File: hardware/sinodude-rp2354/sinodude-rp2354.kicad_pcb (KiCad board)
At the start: 2 copper layers, 75 x 40 mm, 93 parts, among them J1 USB-C, J2 SWD TC2030-IDC latching, J4 DUT, Q1 2N7002, SW1 BOOTSEL, SW2 RESET, U1 RP2354A, U2 AMS1117-3.3, U3 TPS2114APW, U4 SN74LVC8T245PW, U5 SN74LVC1T45DBV, U6 SN74LVC1T45DBV, Y1 12MHz/CL10pF/ESR50R/ABM8-272-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

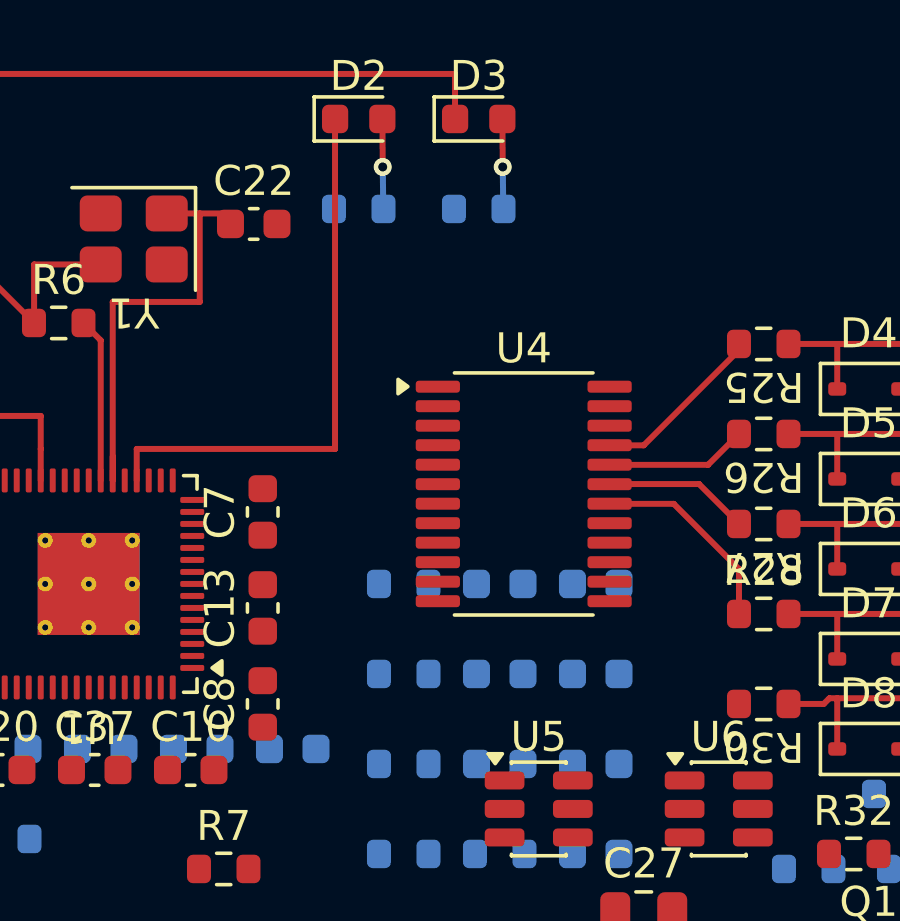
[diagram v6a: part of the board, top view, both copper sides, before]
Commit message: hardware: clear the U1-U4 corridor, route NRST_3V3 and TCK_3V3
Moved C7/C8/C13 out of x=134..140 so the corridor between U1's right pin row
and U4 is clear. Routed NRST_3V3 on top and TCK_3V3 on the bottom through it.

NRST's diagonal originally clipped U4's GND pad 7; it now approaches pin 6
horizontally.

Recorded finding: U1's A-side pin order is the exact reverse of U4's, so the
four-signal bundle has to cross. This is inherent, not a placement mistake -
U1 pin 4 is TCK and pin 8 is NRST, and after the 180 degree rotation that puts
TCK at the bottom of the column while U4 wants it at the top. J4's pin order
matches U4, so the reversal cannot be moved further down the chain either. It
costs roughly 8 vias to resolve in the corridor.

DRC: no shorts, no crossings, no clearance or courtyard violations.
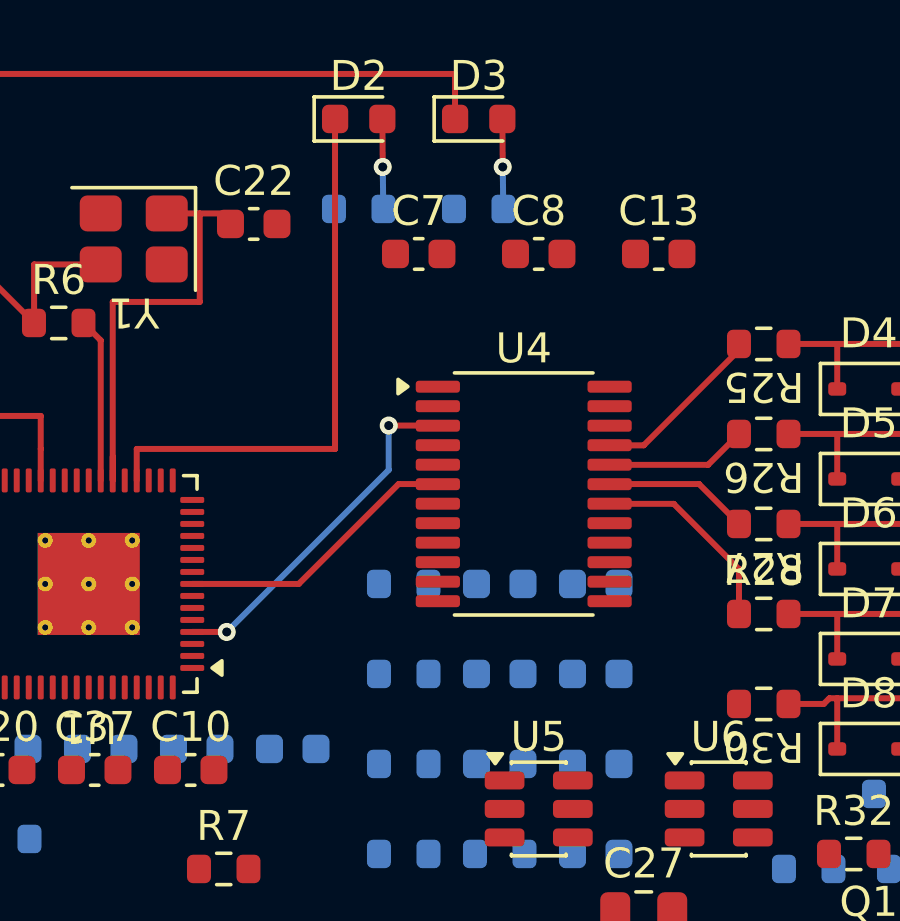
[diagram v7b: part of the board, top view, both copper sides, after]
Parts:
- moved C13 17.7 mm to (149.0, 109.0), turned to 0 degrees
- moved C8 17.6 mm to (145.0, 109.0), turned to 0 degrees
- moved C7 10.0 mm to (141.0, 109.0), turned to 0 degrees
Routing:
- net TCK_3V3: track 0.00 -> 11.9 mm, vias 0 -> 2
- net NRST_3V3: track 0.00 -> 9.57 mm
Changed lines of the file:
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@@
 	(footprint "Capacitor_SMD:C_0603_1608Metric"
 		(layer "F.Cu")
-		(at 135.8 124 90)
+		(at 145 109)
 		(property "Reference" "C8"
-			(at 0 -1.43 90)
+			(at 0 -1.43 0)
 			(unlocked yes)
 			(layer "F.SilkS")
@@
 		)
 		(property "Value" "100nF"
-			(at 0 1.43 90)
+			(at 0 1.43 0)
 			(unlocked yes)
 			(layer "F.SilkS")
@@
 		)
 		(property "Datasheet" ""
-			(at 0 0 90)
+			(at 0 0 0)
 			(layer "F.Fab")
 			(hide yes)
@@
 		)
 		(property "Description" ""
-			(at 0 0 90)
+			(at 0 0 0)
 			(layer "F.Fab")
 			(hide yes)
@@
 		)
 		(fp_text user "${REFERENCE}"
-			(at 0 0 90)
+			(at 0 0 0)
 			(unlocked yes)
 			(layer "F.Fab")
@@
 		)
 		(pad "1" smd roundrect
-			(at -0.775 0 90)
+			(at -0.775 0)
 			(size 0.9 0.95)
 			(layers "F.Cu" "F.Mask" "F.Paste")
@@
 		)
 		(pad "2" smd roundrect
-			(at 0.775 0 90)
+			(at 0.775 0)
 			(size 0.9 0.95)
 			(layers "F.Cu" "F.Mask" "F.Paste")
@@
 	(footprint "Capacitor_SMD:C_0603_1608Metric"
 		(layer "F.Cu")
-		(at 135.8 117.6 90)
+		(at 141 109)
 		(property "Reference" "C7"
-			(at 0 -1.43 90)
+			(at 0 -1.43 0)
 			(unlocked yes)
 			(layer "F.SilkS")
@@
 		)
 		(property "Value" "100nF"
-			(at 0 1.43 90)
+			(at 0 1.43 0)
 			(unlocked yes)
 			(layer "F.SilkS")
@@
 		)
 		(property "Datasheet" ""
-			(at 0 0 90)
+			(at 0 0 0)
 			(layer "F.Fab")
 			(hide yes)
@@
 		)
 		(property "Description" ""
-			(at 0 0 90)
+			(at 0 0 0)
 			(layer "F.Fab")
 			(hide yes)
@@
 		)
 		(fp_text user "${REFERENCE}"
-			(at 0 0 90)
+			(at 0 0 0)
 			(unlocked yes)
 			(layer "F.Fab")
@@
 		)
 		(pad "1" smd roundrect
-			(at -0.775 0 90)
+			(at -0.775 0)
 			(size 0.9 0.95)
 			(layers "F.Cu" "F.Mask" "F.Paste")
@@
 		)
 		(pad "2" smd roundrect
-			(at 0.775 0 90)
+			(at 0.775 0)
 			(size 0.9 0.95)
 			(layers "F.Cu" "F.Mask" "F.Paste")
@@
 	(footprint "Capacitor_SMD:C_0603_1608Metric"
 		(layer "F.Cu")
-		(at 135.8 120.8 90)
+		(at 149 109)
 		(property "Reference" "C13"
-			(at 0 -1.43 90)
+			(at 0 -1.43 0)
 			(unlocked yes)
 			(layer "F.SilkS")
@@
 		)
 		(property "Value" "100nF"
-			(at 0 1.43 90)
+			(at 0 1.43 0)
 			(unlocked yes)
 			(layer "F.SilkS")
@@
 		)
 		(property "Datasheet" ""
-			(at 0 0 90)
+			(at 0 0 0)
 			(layer "F.Fab")
 			(hide yes)
@@
 		)
 		(property "Description" ""
-			(at 0 0 90)
+			(at 0 0 0)
 			(layer "F.Fab")
 			(hide yes)
@@
 		)
 		(fp_text user "${REFERENCE}"
-			(at 0 0 90)
+			(at 0 0 0)
 			(unlocked yes)
 			(layer "F.Fab")
@@
 		)
 		(pad "1" smd roundrect
-			(at -0.775 0 90)
+			(at -0.775 0)
 			(size 0.9 0.95)
 			(layers "F.Cu" "F.Mask" "F.Paste")
@@
 		)
 		(pad "2" smd roundrect
-			(at 0.775 0 90)
+			(at 0.775 0)
 			(size 0.9 0.95)
 			(layers "F.Cu" "F.Mask" "F.Paste")
@@
 	)
 	(segment
+		(start 133.449999 121.6)
+		(end 134.6 121.6)
+		(width 0.2)
+		(layer "F.Cu")
+		(net "TCK_3V3")
+	)
+	(segment
+		(start 140 114.72)
+		(end 141.64 114.72)
+		(width 0.2)
+		(layer "F.Cu")
+		(net "TCK_3V3")
+	)
+	(via
+		(at 134.6 121.6)
+		(size 0.6)
+		(drill 0.3)
+		(layers "F.Cu" "B.Cu")
+		(net "TCK_3V3")
+	)
+	(via
+		(at 140 114.72)
+		(size 0.6)
+		(drill 0.3)
+		(layers "F.Cu" "B.Cu")
+		(net "TCK_3V3")
+	)
+	(segment
+		(start 134.6 121.6)
+		(end 140 116.2)
+		(width 0.2)
+		(layer "B.Cu")
+		(net "TCK_3V3")
+	)
+	(segment
+		(start 140 116.2)
+		(end 140 114.72)
+		(width 0.2)
+		(layer "B.Cu")
+		(net "TCK_3V3")
+	)
+	(segment
+		(start 137 120)
+		(end 140.33 116.67)
+		(width 0.2)
+		(layer "F.Cu")
+		(net "NRST_3V3")
+	)
+	(segment
+		(start 140.33 116.67)
+		(end 141.64 116.67)
+		(width 0.2)
+		(layer "F.Cu")
+		(net "NRST_3V3")
+	)
+	(segment
+		(start 133.449999 120)
+		(end 137 120)
+		(width 0.2)
+		(layer "F.Cu")
+		(net "NRST_3V3")
+	)
+	(segment

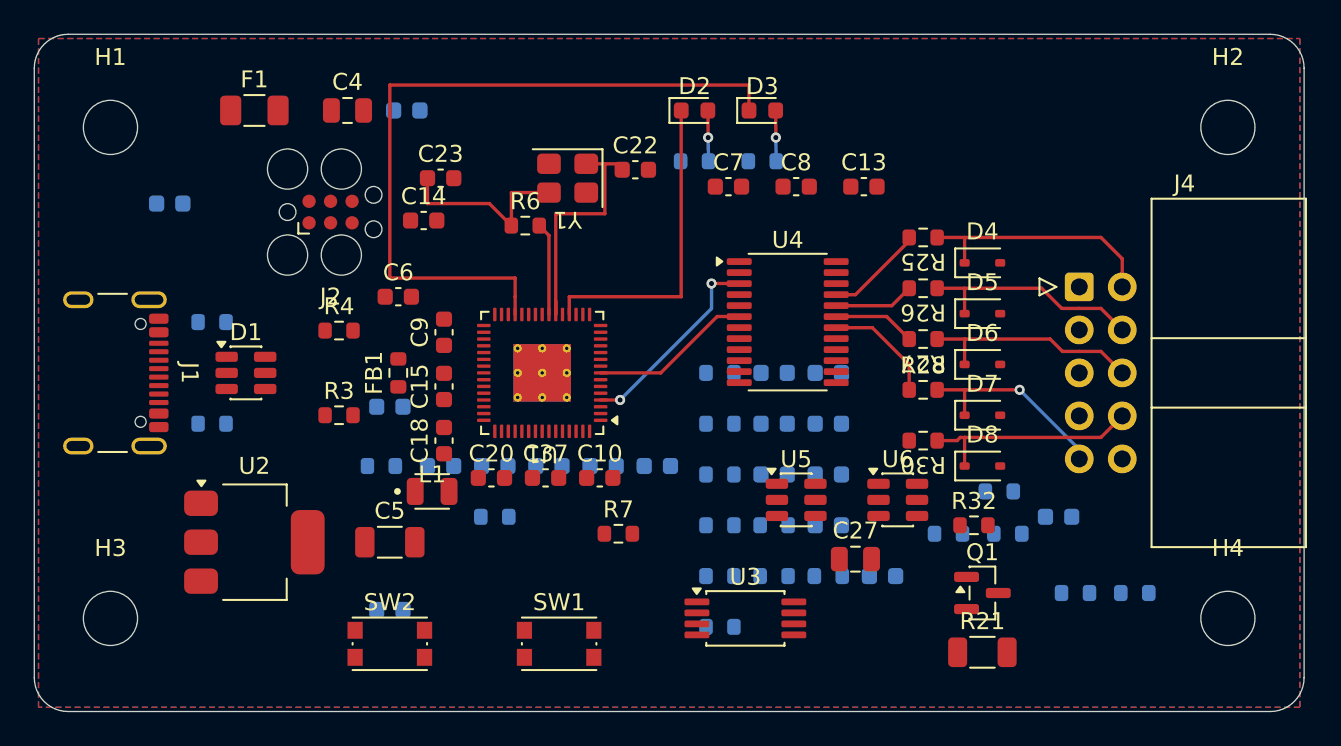
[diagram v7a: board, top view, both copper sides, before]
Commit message: hardware: route 48 links with a scripted geometry router
Built a local router: s-expression parser, pad-position model, spatial
clearance checker, and a 45-degree path search. It computes 128 links needed,
independently matching DRC's 130 unconnected items, and reproduces every pad
position against values previously confirmed over KiCad's live IPC.

Appended 170 segments and 25 vias directly to the board file. Unconnected
drops 130 -> 83.

Three bugs the model-vs-DRC cross-check caught, each validated on a copy
before touching the real board:
- Clearance formula was short by exactly 0.1 mm: trace obstacles were stored
  with w/2 - TW/2, making the requirement CLR + w1/2 + w2/2 - 0.1.
- A 0.15 mm fine-trace fallback undercut the board minimum (37 violations).
- 0.4 mm power traces cannot leave U1's 0.4 mm-pitch pads: centred on a pad,
  a 0.4 mm trace leaves 0.1 mm to its neighbour. Power is now 0.2 mm, which
  still carries the 500 mA the input fuse allows.

Also found: J1's VBUS pins A4/B4 are physically coincident in the USB-C
footprint, so that link needed no trace at all.

DRC: no shorts, no crossings, no clearance and no track-width violations.
Remaining 24 are all pre-existing: U1 thermal via drill, J1 footprint-internal
hole clearance, and thermal-relief spoke counts.
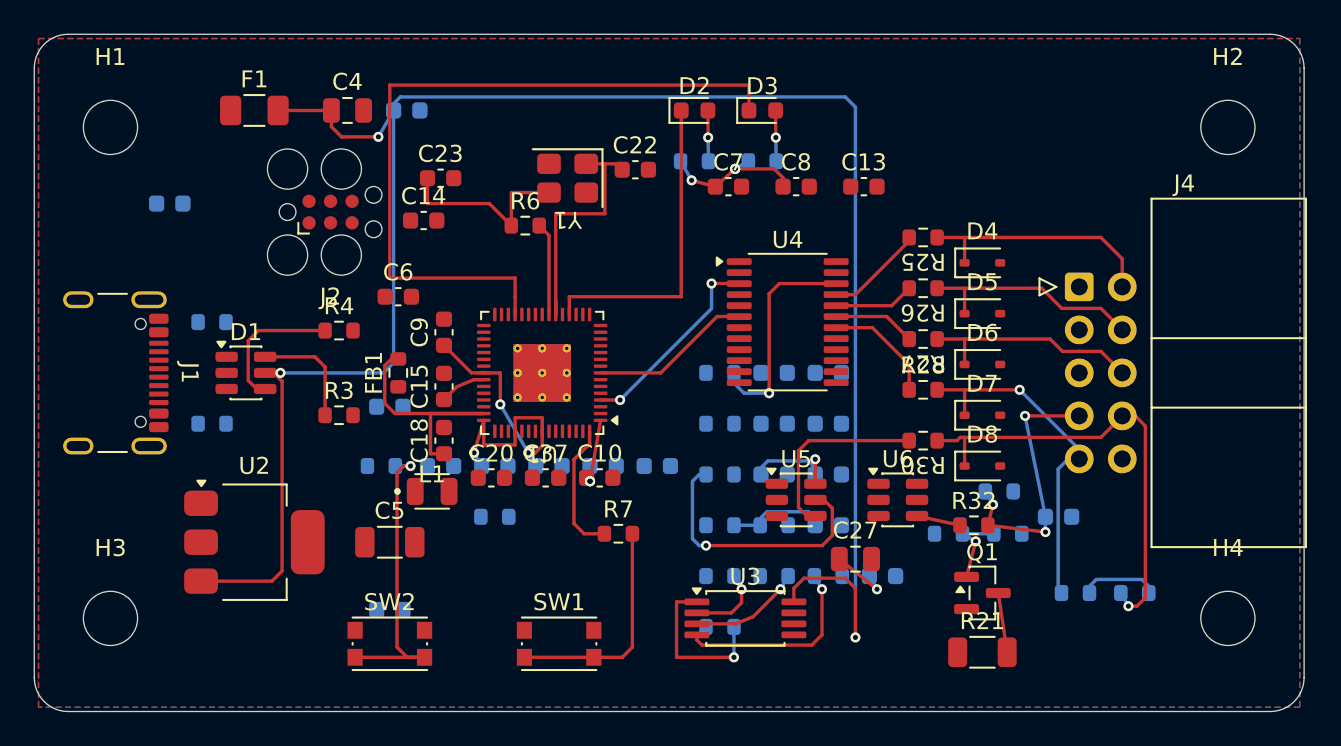
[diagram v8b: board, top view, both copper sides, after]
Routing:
- net +5V: track 0.00 -> 116.4 mm, vias 0 -> 3
- net +3V3: track 0.00 -> 38.4 mm, vias 0 -> 8
- net RUN: track 0.00 -> 18.1 mm, vias 0 -> 1
- net DATA_DIR: track 0.00 -> 15.8 mm, vias 0 -> 1
- net Net-(J4-Pin_7): track 0.00 -> 15.8 mm, vias 0 -> 3
- net ADC_AVDD: track 0.00 -> 15.6 mm
- net VTGT: track 0.00 -> 15.1 mm, vias 0 -> 2
- net Net-(D8-A1): track 13.2 -> 27.1 mm, vias 0 -> 1
- net Net-(R7-Pad2): track 0.00 -> 13.3 mm
- net XLAT_OE: track 0.00 -> 13.0 mm, vias 0 -> 1
- net Net-(U3-ILIM): track 0.00 -> 11.7 mm, vias 0 -> 1
- net DATA_B: track 0.00 -> 11.3 mm
- net VTGT_STAT: track 0.00 -> 9.66 mm, vias 0 -> 1
- net Net-(D7-A1): track 11.9 -> 20.9 mm
- net Net-(D1-I/O2-Pad4): track 0.00 -> 8.34 mm
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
